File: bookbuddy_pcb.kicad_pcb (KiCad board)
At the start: 2 copper layers, 68.5 x 15 mm, 46 parts, among them IC1 APX803S-31SA-7, J1 Conn_01x04_Socket, J2 10164359-00011LF, Q1 BSS806NEH6327XTSA1, Q2 DMG2305UX, SW1 SW_Push, SW2 SW_Push, SW3 Power Switch, U1 ESP32-C3-MINI-1, U2 MLX90393SLW-ABA-011-RE, U3 MIC5365-3.3YC5-TR, U4 MCP73832, Y1 32.768kHz

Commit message: added test points
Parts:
- added 3v3: +3v3, TestPoint:TestPoint_Pad_1.0x1.0mm, B.Cu at (115.0, 90.5)
- added BATT: BATT, TestPoint:TestPoint_Pad_1.0x1.0mm, B.Cu at (107.5, 99.5)
- added GND: GND, TestPoint:TestPoint_Pad_1.0x1.0mm, B.Cu at (113.0, 90.5)
- added SCL: SCL, TestPoint:TestPoint_Pad_1.0x1.0mm, B.Cu at (144.5, 98.5)
- added SDA: SDA, TestPoint:TestPoint_Pad_1.0x1.0mm, B.Cu at (142.0, 98.5)
- added VBUS: VBUS, TestPoint:TestPoint_Pad_1.0x1.0mm, B.Cu at (110.0, 99.5)
- moved R3 0.50 mm to (146.5, 98.0)
- moved R4 0.50 mm to (148.5, 98.0)
- moved C10 0.47 mm to (140.0, 98.0)
- moved C11 0.47 mm to (138.0, 98.0)
- moved C12 0.47 mm to (129.0, 98.0)
- moved C13 0.47 mm to (131.0, 98.0)
- moved U3 0.47 mm to (134.5, 98.0)

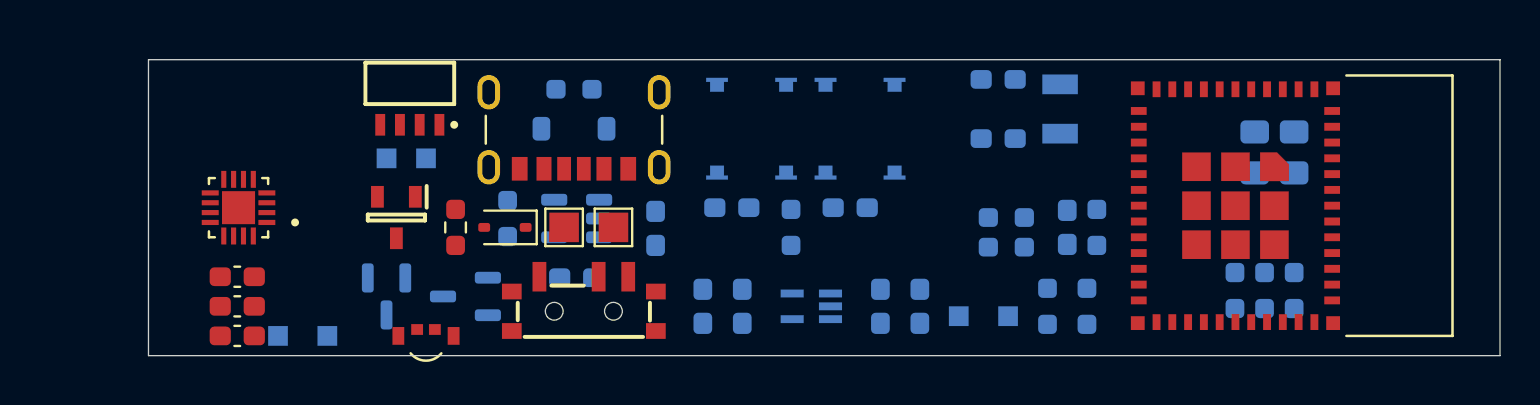
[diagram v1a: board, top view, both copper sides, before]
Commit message: updated pcb layout quickly
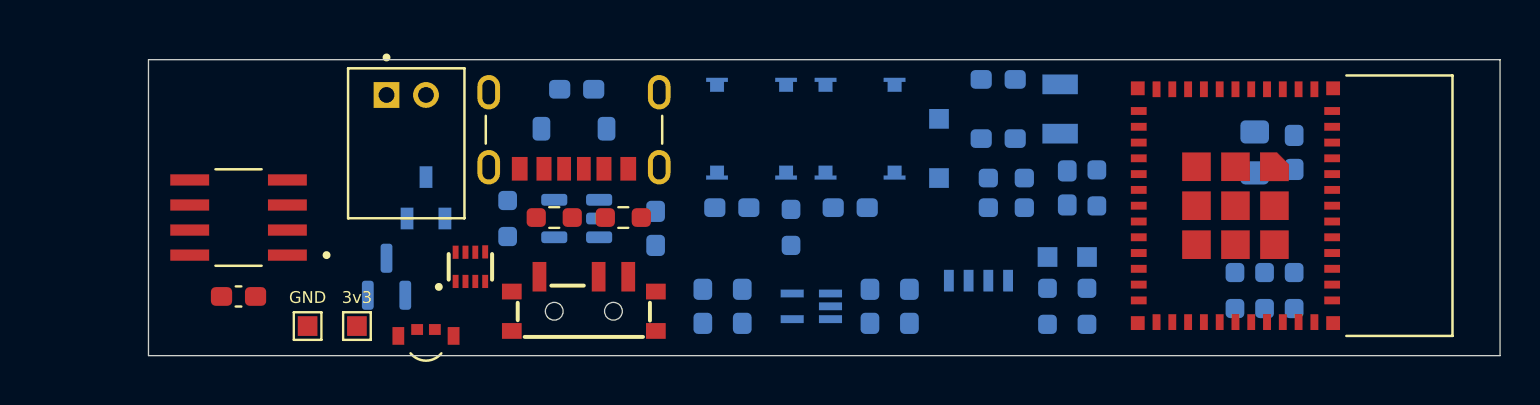
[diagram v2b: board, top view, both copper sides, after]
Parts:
- removed C8: 0.1uF, Capacitor_SMD:C_0603_1608Metric_Pad1.08x0.95mm_HandSolder
- removed C9: 4.7uF, Capacitor_SMD:C_0603_1608Metric_Pad1.08x0.95mm_HandSolder
- removed D3: SD103AWS-TP, Diode_SMD:D_SOD-323
- removed Q2: DMG2305UX, Package_TO_SOT_SMD:SOT-23-3
- removed R8: 10k, Resistor_SMD:R_0603_1608Metric_Pad0.98x0.95mm_HandSolder
- removed R9: 1k, Resistor_SMD:R_0603_1608Metric_Pad0.98x0.95mm_HandSolder
- removed TP1: BATT PAD, TestPoint:TestPoint_Pad_1.5x1.5mm
- removed TP2: GND PAD, TestPoint:TestPoint_Pad_1.5x1.5mm
- removed U2: MLX90393SLW-ABA-011-RE, bookbuddy:QFN50P300X300X100-17N
- added IC2: LM66200DRLR, bookbuddy:SOT8, F.Cu at (117.2, 96.0)
- added J3: Battery Connector, bookbuddy:JST_S2B-PH-K-S_LF__SN_, F.Cu at (114.0, 87.3)
- added R13: 5.1k, Resistor_SMD:R_0603_1608Metric_Pad0.98x0.95mm_HandSolder, F.Cu at (121.5, 93.5)
- added R14: 5.1k, Resistor_SMD:R_0603_1608Metric_Pad0.98x0.95mm_HandSolder, F.Cu at (125.0, 93.5)
- added U5: MLX90395KDC-BBA-101-RE, bookbuddy:SOIC127P600X172-8N, F.Cu at (105.5, 93.5)
- 3v3, GND: moved to F.Cu
- C5: value 10uF -> 0.1uF; footprint Capacitor_SMD:C_0805_2012Metric_Pad1.18x1.45mm_HandSolder -> Capacitor_SMD:C_0603_1608Metric_Pad1.08x0.95mm_HandSolder
- IC1: value APX803S-31SA-7 -> APX810S-31SA-7; moved to B.Cu
- J1: moved to B.Cu
- Q1: value BSS806NEH6327XTSA1 -> DMG2305UX-13
- R11: value 328K 0.1% -> 100K 0.1%
- R12: value 820k 0.1% -> 249k 0.1%
- moved BATT 35.3 mm to (141.0, 88.5)
- moved VBUS 32.0 mm to (141.0, 91.5)
- moved J1 29.9 mm to (143.0, 96.7)
- moved C15 9.55 mm to (122.6, 87.0), turned to 180 degrees
- moved GND 9.39 mm to (109.0, 99.0), turned to 0 degrees
- moved 3v3 9.19 mm to (111.5, 99.0), turned to 0 degrees
- moved SDA 7.16 mm to (148.5, 95.5)
- moved SCL 3.61 mm to (146.5, 95.5)
- moved C7 2.00 mm to (105.5, 97.5), turned to 0 degrees
- moved C14 2.00 mm to (147.5, 92.0)
- moved R11 2.00 mm to (144.4, 91.5)
- moved R12 2.00 mm to (144.4, 93.0)
- moved R2 2.00 mm to (149.0, 92.0)
- moved IC1 1.80 mm to (115.0, 92.5), turned to 90 degrees
- moved Q1 1.00 mm to (113.0, 96.5), turned to 90 degrees
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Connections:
- J2 pad A5: unconnected-(J2-CC1-PadA5) -> Net-(J2-CC1)
- J2 pad B5: unconnected-(J2-CC2-PadB5) -> Net-(J2-CC2)
- J2 pad SH1: unconnected-(J2-SHIELD-PadSH1)_2 -> GND
- J2 pad SH2: unconnected-(J2-SHIELD-PadSH1) -> GND
- J2 pad SH3: unconnected-(J2-SHIELD-PadSH1)_0 -> GND
- J2 pad SH4: unconnected-(J2-SHIELD-PadSH1)_1 -> GND
- Q1 pad 1: +BATT -> /charging/BATT_PROT
- Q1 pad 3: /charging/BATT_PROT -> +BATT

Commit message: addressed Craig's comments
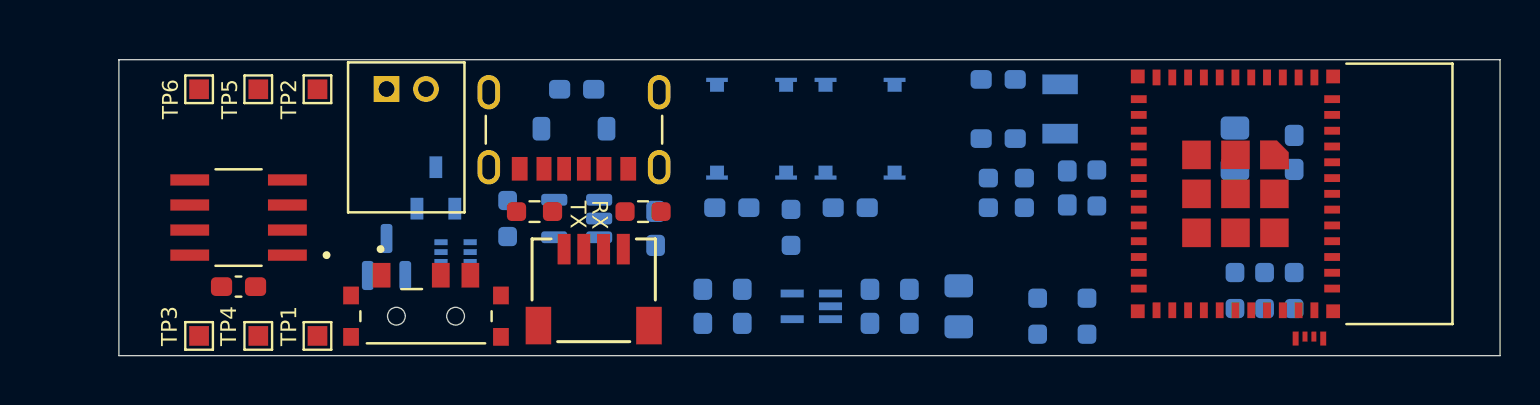
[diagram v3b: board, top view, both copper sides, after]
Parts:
- removed D1: IN-S126TASRGB, bookbuddy:LED_IN-S126TASRGB
- added C4: DNP, Capacitor_SMD:C_0805_2012Metric_Pad1.18x1.45mm_HandSolder, B.Cu at (156.0, 90.0)
- added LED1: IN-S63TBS5R5G5B, bookbuddy:IN-S63TBS5R5G5B_INO, F.Cu at (159.8, 99.9)
- IC2: moved to B.Cu
- J1: value Conn_01x04_Socket -> SM04B-SRSS-TB; footprint bookbuddy:GCT_BC075-04-A-L-A_REVC2 -> bookbuddy:CONN_SM04B-SRSS-TB_JST; moved to F.Cu
- R5: value 27 -> 240
- R6: value 27 -> 39
- R7: value 91 -> 39
- SW3: value Power Switch -> SLW-66527511-SMT-TR; footprint bookbuddy:CUS-12B -> bookbuddy:SW_SLW-66527511-SMT-TR
- TP1: renamed from SCL; moved to F.Cu
- TP2: renamed from SDA; moved to F.Cu
- TP5: renamed from BATT; moved to F.Cu
- TP6: renamed from VBUS; moved to F.Cu
- U3: value MIC5365-3.3YC5-TR -> MIC5504-3.3YM5-TR
- moved TP2 39.9 mm to (109.5, 87.0), turned to 90 degrees
- moved TP6 37.8 mm to (103.5, 87.0), turned to 90 degrees
- moved TP1 37.2 mm to (109.5, 99.5), turned to 90 degrees
- moved TP5 34.5 mm to (106.5, 87.0), turned to 90 degrees
- moved J1 19.5 mm to (123.5, 97.2)
- moved C6 16.9 mm to (142.0, 98.0)
- moved TP3 8.02 mm to (103.5, 99.5)
- moved SW3 8.00 mm to (115.0, 98.5)
- moved TP4 2.55 mm to (106.5, 99.5)
- moved R8 1.04 mm to (126.0, 93.2)
- moved R9 1.04 mm to (120.5, 93.2)
- moved Q1 1.00 mm to (113.0, 95.5)
- moved IC2 0.90 mm to (116.5, 95.5), turned to -90 degrees
- moved IC1 0.71 mm to (115.5, 92.0)
- moved R3 0.71 mm to (146.0, 98.5)
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- renumbered C11 to C10, C12 to C11, C13 to C12, C14 to C13, C15 to C14, C16 to C15, C4 to C6, C6 to C7, C7 to C8, C10 to C9, R14 to R8, R13 to R9, 3v3 to TP3, GND to TP4, U5 to U2
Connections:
- J3 pad 1: Net-(J3-Pin_1) -> +BATT
- R5 pad 1: /mcu/B_LED -> /mcu/G_LED
- R6 pad 1: /mcu/G_LED -> /charging/CHG_STAT
- R7 pad 1: /charging/CHG_STAT -> /mcu/B_LED
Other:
- board size 68.5 x 15 mm -> 70 x 15 mm
- board text added: "70mm"
- board text added: "Domenic Hampson Aug-11-2025 Book Buddy Rev A"
- board text added: "Edge for mounting"
- board text added: "RX"
- board text added: "TX"
- board text removed: "68.5mm"

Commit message: Added fuse
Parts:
- added F1: Fuse_Small, bookbuddy:FUSC0402X49N, F.Cu at (109.5, 90.5)
- U3: footprint bookbuddy:SOT65P210X110-5N -> Package_TO_SOT_SMD:SOT-23-5_HandSoldering
- moved C8 3.48 mm to (102.0, 96.9)
- moved U2 3.48 mm to (102.0, 93.4)
- moved 3v3 3.00 mm to (100.5, 99.5)
- moved BATT 3.00 mm to (103.5, 87.0)
- moved GND 3.00 mm to (103.5, 99.5)
- moved SCL 3.00 mm to (106.5, 99.5)
- moved SDA 3.00 mm to (106.5, 87.0)
- moved VBUS 3.00 mm to (100.5, 87.0)
- moved R11 1.56 mm to (144.0, 93.0)
- moved R12 1.56 mm to (144.0, 94.5)
- moved C13 1.00 mm to (147.5, 93.0)
- moved R2 1.00 mm to (149.0, 93.0)
- moved SW3 0.50 mm to (115.0, 99.0)
- moved LED1 0.47 mm to (159.8, 100.4)
- moved C1 0.36 mm to (144.0, 86.9)
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- renumbered TP3 to 3v3, TP5 to BATT, TP4 to GND, TP1 to SCL, TP2 to SDA, TP6 to VBUS
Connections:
- J3 pad 1: +BATT -> Net-(J3-Pin_1)
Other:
- board size 70 x 15 mm -> 74 x 15.5 mm
- board text added: "15.5mm"
- board text removed: "15mm"

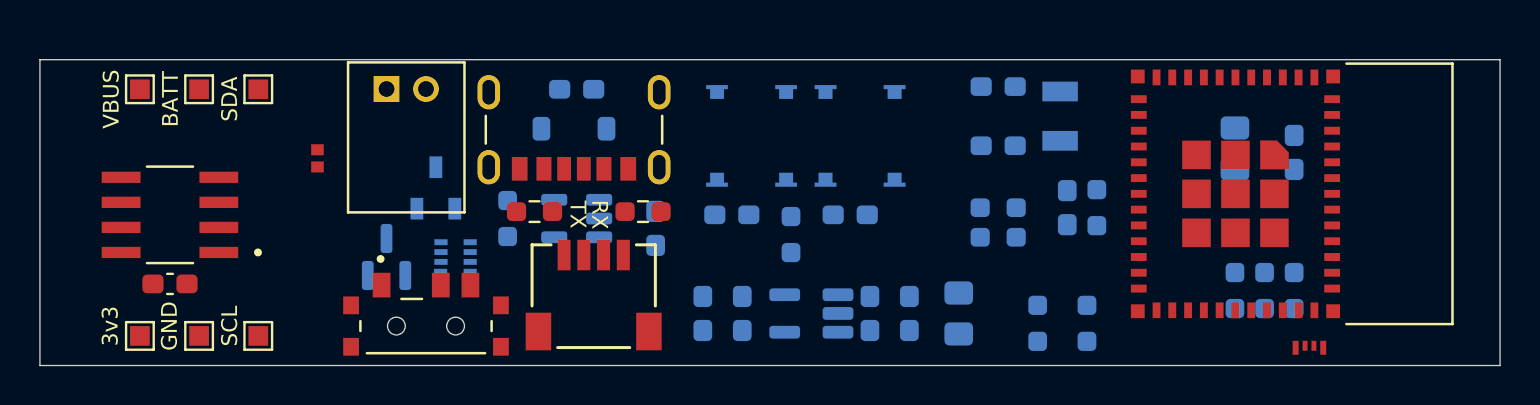
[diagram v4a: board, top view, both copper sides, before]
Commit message: switched to 4 layer
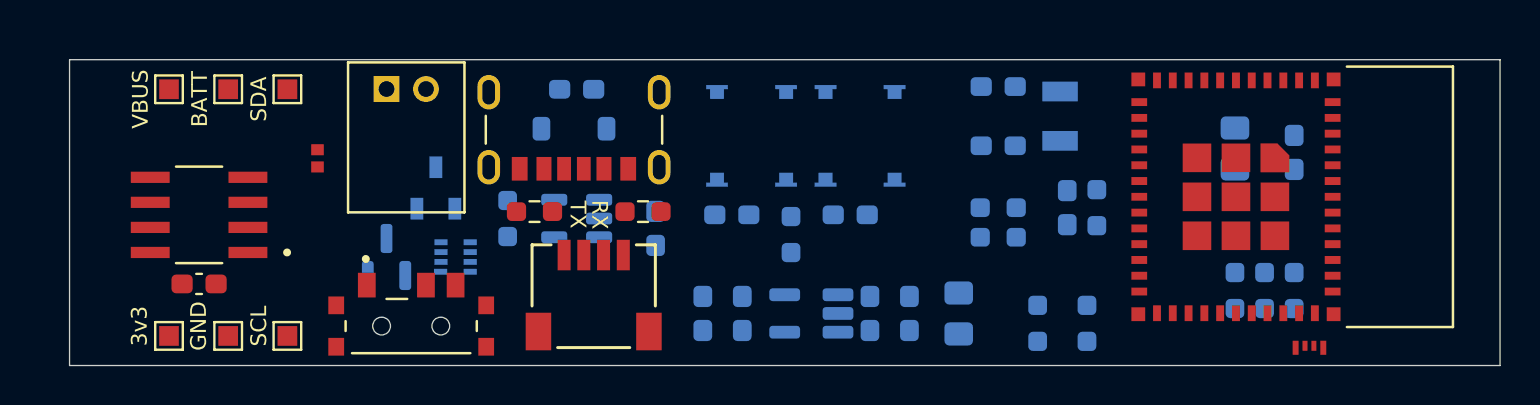
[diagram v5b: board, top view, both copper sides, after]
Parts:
- moved 3v3 1.47 mm to (102.0, 99.5)
- moved BATT 1.47 mm to (105.0, 87.0)
- moved C8 1.47 mm to (103.5, 96.9)
- moved GND 1.47 mm to (105.0, 99.5)
- moved SCL 1.47 mm to (108.0, 99.5)
- moved SDA 1.47 mm to (108.0, 87.0)
- moved U2 1.47 mm to (103.5, 93.4)
- moved VBUS 1.47 mm to (102.0, 87.0)
- moved SW3 0.75 mm to (114.2, 99.0)
- moved U1 0.15 mm to (158.8, 92.5)
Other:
- board size 74 x 15.5 mm -> 72.5 x 15.5 mm
- copper layers 2 -> 4
- board text added: "72.5mm"
- board text removed: "70mm"
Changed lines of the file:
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@@
 	(layers
 		(0 "F.Cu" signal)
+		(1 "In1.Cu" power)
+		(2 "In2.Cu" power)
 		(31 "B.Cu" signal)
 		(32 "B.Adhes" user "B.Adhesive")
@@
 	)
 	(setup
+		(stackup
+			(layer "F.SilkS"
+				(type "Top Silk Screen")
+			)
+			(layer "F.Paste"
+				(type "Top Solder Paste")
+			)
+			(layer "F.Mask"
+				(type "Top Solder Mask")
+				(thickness 0.01)
+			)
+			(layer "F.Cu"
+				(type "copper")
+				(thickness 0.035)
+			)
+			(layer "dielectric 1"
+				(type "prepreg")
+				(thickness 0.1)
+				(material "FR4")
+				(epsilon_r 4.5)
+				(loss_tangent 0.02)
+			)
+			(layer "In1.Cu"
+				(type "copper")
+				(thickness 0.035)
+			)
+			(layer "dielectric 2"
+				(type "core")
+				(thickness 1.24)
+				(material "FR4")
+				(epsilon_r 4.5)
+				(loss_tangent 0.02)
+			)
+			(layer "In2.Cu"
+				(type "copper")
+				(thickness 0.035)
+			)
+			(layer "dielectric 3"
+				(type "prepreg")
+				(thickness 0.1)
+				(material "FR4")
+				(epsilon_r 4.5)
+				(loss_tangent 0.02)
+			)
+			(layer "B.Cu"
+				(type "copper")
+				(thickness 0.035)
+			)
+			(layer "B.Mask"
+				(type "Bottom Solder Mask")
+				(thickness 0.01)
+			)
+			(layer "B.Paste"
+				(type "Bottom Solder Paste")
+			)
+			(layer "B.SilkS"
+				(type "Bottom Silk Screen")
+			)
+			(copper_finish "None")
+			(dielectric_constraints no)
+		)
 		(pad_to_mask_clearance 0)
 		(allow_soldermask_bridges_in_footprints no)
@@
 	(footprint "TestPoint:TestPoint_Pad_1.0x1.0mm"
 		(layer "F.Cu")
-		(at 103.5 99.5)
+		(at 104.975 99.5)
 		(descr "SMD rectangular pad as test Point, square 1.0mm side length")
 		(tags "test point SMD pad rectangle square")
@@
 	(footprint "bookbuddy:SW_SLW-66527511-SMT-TR"
 		(layer "F.Cu")
-		(at 115 99)
+		(at 114.25 99)
 		(property "Reference" "SW3"
 			(at -1.325 -5.875 0)
@@
 	(footprint "bookbuddy:XCVR_ESP32-C3-MINI-1-N4"
 		(layer "F.Cu")
-		(at 158.725 92.3 -90)
+		(at 158.75 92.45 -90)
 		(property "Reference" "U1"
 			(at -3.675 -9.635 90)
@@
 			(polygon
 				(pts
-					(xy 167.025 85.7) (xy 167.025 98.9) (xy 161.625 98.9) (xy 161.625 85.7)
+					(xy 167.05 85.85) (xy 167.05 99.05) (xy 161.65 99.05) (xy 161.65 85.85)
 				)
 			)
@@
 			(polygon
 				(pts
-					(xy 167.025 85.7) (xy 167.025 98.9) (xy 161.625 98.9) (xy 161.625 85.7)
+					(xy 167.05 85.85) (xy 167.05 99.05) (xy 161.65 99.05) (xy 161.65 85.85)
 				)
 			)
@@
 			(polygon
 				(pts
-					(xy 167.025 85.7) (xy 167.025 98.9) (xy 161.625 98.9) (xy 161.625 85.7)
+					(xy 167.05 85.85) (xy 167.05 99.05) (xy 161.65 99.05) (xy 161.65 85.85)
 				)
 			)
@@
 	(footprint "TestPoint:TestPoint_Pad_1.0x1.0mm"
 		(layer "F.Cu")
-		(at 100.5 87 90)
+		(at 101.975 87 90)
 		(descr "SMD rectangular pad as test Point, square 1.0mm side length")
 		(tags "test point SMD pad rectangle square")
@@
 	(footprint "TestPoint:TestPoint_Pad_1.0x1.0mm"
 		(layer "F.Cu")
-		(at 100.5 99.5)
+		(at 101.975 99.5)
 		(descr "SMD rectangular pad as test Point, square 1.0mm side length")
 		(tags "test point SMD pad rectangle square")
@@
 	(footprint "TestPoint:TestPoint_Pad_1.0x1.0mm"
 		(layer "F.Cu")
-		(at 106.5 87 90)
+		(at 107.975 87 90)
 		(descr "SMD rectangular pad as test Point, square 1.0mm side length")
 		(tags "test point SMD pad rectangle square")
@@
 	(footprint "Capacitor_SMD:C_0603_1608Metric_Pad1.08x0.95mm_HandSolder"
 		(layer "F.Cu")
-		(at 102.025 96.865)
+		(at 103.5 96.865)
 		(descr "Capacitor SMD 0603 (1608 Metric), square (rectangular) end terminal, IPC_7351 nominal with elongated pad for handsoldering. (Body size source: IPC-SM-782 page 76, https://www.pcb-3d.com/wordpress/wp-content/uploads/ipc-sm-782a_amendment_1_and_2.pdf), generated with kicad-footprint-generator")
 		(tags "capacitor handsolder")
@@
 	(footprint "bookbuddy:SOIC127P600X172-8N"
 		(layer "F.Cu")
-		(at 102.025 93.365 180)
+		(at 103.5 93.365 180)
 		(property "Reference" "U2"
 			(at 0 -3.5 0)
@@
 	(footprint "TestPoint:TestPoint_Pad_1.0x1.0mm"
 		(layer "F.Cu")
-		(at 103.5 87 90)
+		(at 104.975 87 90)
 		(descr "SMD rectangular pad as test Point, square 1.0mm side length")
 		(tags "test point SMD pad rectangle square")
@@
 	(footprint "TestPoint:TestPoint_Pad_1.0x1.0mm"
 		(layer "F.Cu")
-		(at 106.5 99.5 90)
+		(at 107.975 99.5 90)
 		(descr "SMD rectangular pad as test Point, square 1.0mm side length")
 		(tags "test point SMD pad rectangle square")
@@
 	)
 	(gr_rect
-		(start 95.5 85.5)
-		(end 97.5 101)
+		(start 97 85.5)
+		(end 99 101)
 		(stroke
 			(width 0.1)
@@
 	)
 	(gr_rect
-		(start 97.46 88.365)
-		(end 106.845 97.965)
+		(start 98.935 88.365)
+		(end 108.32 97.965)
 		(stroke
 			(width 0.1)
@@
 	)
 	(gr_rect
-		(start 95.435 85.5)
+		(start 96.935 85.5)
 		(end 169.435 101)
 		(stroke
@@
 	)
 	(gr_text "Domenic Hampson\nAug-11-2025\nBook Buddy Rev A"
-		(at 103.5 87.5 -0)
+		(at 109 89.5 0)
 		(layer "B.SilkS")
 		(effects
 			(font
-				(size 0.4 0.4)
-				(thickness 0.075)
+				(size 0.8 0.8)
+				(thickness 0.15)
 				(bold yes)
 			)
@@
 		)
 	)
-	(gr_text "70mm\n"
-		(at 134 84.3625 0)
+	(gr_text "72.5mm\n"
+		(at 132 84.3625 0)
 		(layer "Dwgs.User")
 		(effects
@@
 	)
 	(gr_text "Keep out zone"
-		(at 100.025 89.865 0)
+		(at 101.5 89.865 0)
 		(layer "User.1")
 		(effects

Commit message: finished routing the pcb
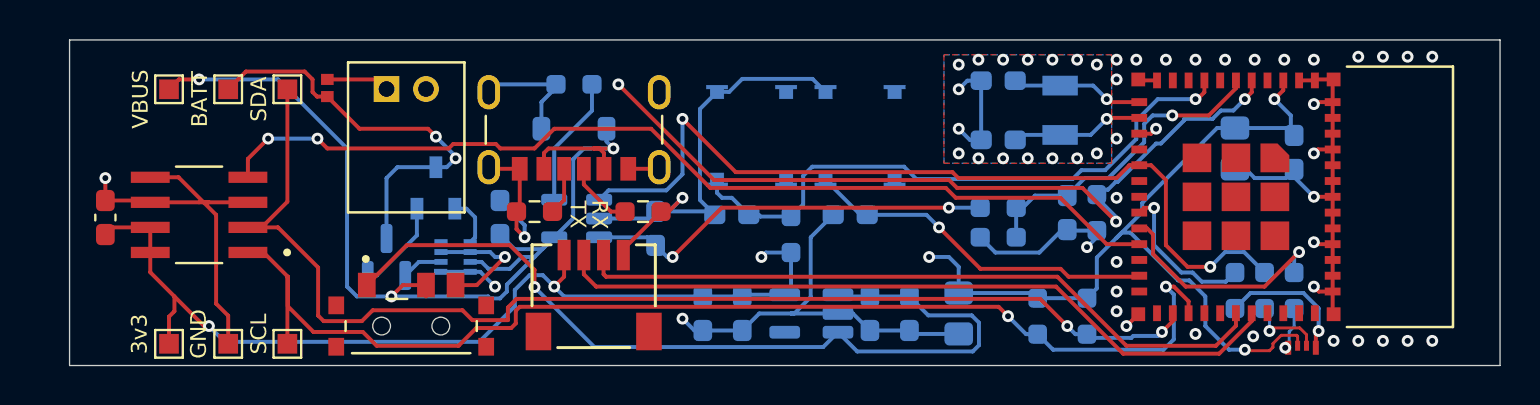
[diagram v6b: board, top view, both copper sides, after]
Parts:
- moved R10 7.59 mm to (122.5, 86.8), turned to 0 degrees
- moved C14 7.57 mm to (118.8, 93.5), turned to 90 degrees
- moved C8 5.82 mm to (98.8, 93.5), turned to 90 degrees
- moved F1 3.60 mm to (110.0, 86.9)
- moved 3v3 0.40 mm to (102.0, 99.9)
- moved GND 0.40 mm to (105.0, 99.9)
- moved SCL 0.40 mm to (108.0, 99.9)
- moved LED1 0.37 mm to (159.4, 100.4)
- moved R3 0.36 mm to (146.0, 98.5)
- moved R4 0.36 mm to (148.5, 98.5)
- moved C1 0.30 mm to (144.0, 86.6)
- moved C2 0.30 mm to (144.0, 89.6)
- moved Y1 0.30 mm to (147.1, 88.1)
- moved C13 0.25 mm to (147.5, 93.2)
- moved R2 0.25 mm to (149.0, 93.2)
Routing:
- net GND: track 0.00 -> 127.0 mm, vias 0 -> 54
- net VBUS: track 0.00 -> 93.4 mm, vias 0 -> 6
- net +3.3V: track 0.00 -> 91.0 mm, vias 0 -> 6
- net /hall_effect/SDA: track 0.00 -> 61.6 mm, vias 0 -> 2
- net /hall_effect/SCL: track 0.00 -> 60.4 mm, vias 0 -> 2
- net /hall_effect/TRIG: track 0.00 -> 49.8 mm, vias 0 -> 2
- net Net-(SW3-B): track 0.00 -> 44.2 mm, vias 0 -> 1
- net /charging/CHG_STAT: track 0.00 -> 43.4 mm, vias 0 -> 2
- net +BATT: track 0.00 -> 41.9 mm, vias 0 -> 4
- net /mcu/TX: track 0.00 -> 37.6 mm
- net /mcu/RX: track 0.00 -> 35.6 mm
- net Net-(U1-EN/CHIP_PU): track 0.00 -> 31.0 mm, vias 0 -> 1
- net Net-(U1-GPIO9): track 0.00 -> 18.0 mm, vias 0 -> 1
- net /charging/BATT_V: track 0.00 -> 16.1 mm, vias 0 -> 1
- net /mcu/B_LED: track 0.00 -> 11.8 mm, vias 0 -> 1
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- added copper zone on In2.Cu, net +3.3V
- added copper zone on In2.Cu, net +BATT
- added copper zone on B.Cu, net GND
- added copper zone on F.Cu, net GND
- added copper zone on In1.Cu, net GND
- added copper zone on In2.Cu, net VBUS
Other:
- board size 72.5 x 15.5 mm -> 72.5 x 16.5 mm
- board text added: "Too close to sensor?"
